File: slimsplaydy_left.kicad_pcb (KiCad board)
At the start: 2 copper layers, 122.6 x 97.5 mm, 37 parts

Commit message: some ideas and how-tos
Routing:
- net GND: track 50.8 -> 0.09 mm, vias 9 -> 16
- net finger_middle_bottom: track 122.0 -> 106.1 mm
- net finger_inner_home: track 71.0 -> 77.8 mm
- net BAT_P: track 68.7 -> 62.7 mm, vias 2 -> 4
- net thumb_tucky_fan: track 61.6 -> 64.2 mm
- net RAW: track 69.8 -> 71.8 mm, vias 2 -> 4
- net finger_inner_top: track 17.2 -> 15.4 mm
- net finger_index_bottom: track 78.6 -> 80.1 mm
- net thumb_reachy_fan: track 47.2 -> 48.4 mm
- net RST: track 64.1 -> 63.3 mm
- net finger_pinky_bottom: track 142.8 -> 143.3 mm
- added copper zone on F.Cu, net BAT_P
- added copper zone on B.Cu, net RAW
- added copper zone on F.Cu, net RAW
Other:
- outline, holes or cut-outs redrawn

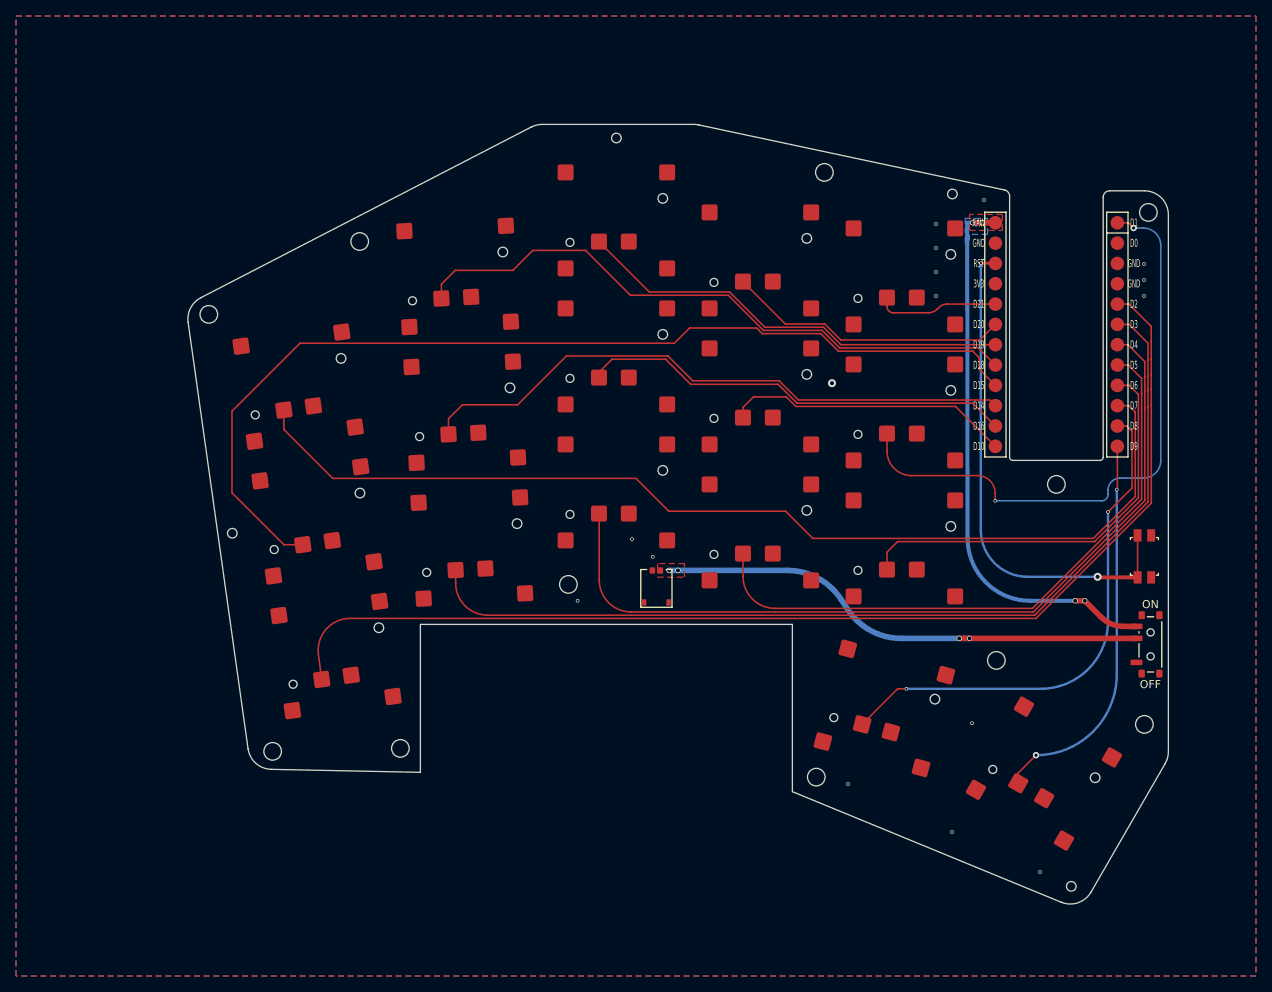
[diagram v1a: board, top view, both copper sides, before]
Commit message: fixed cutout
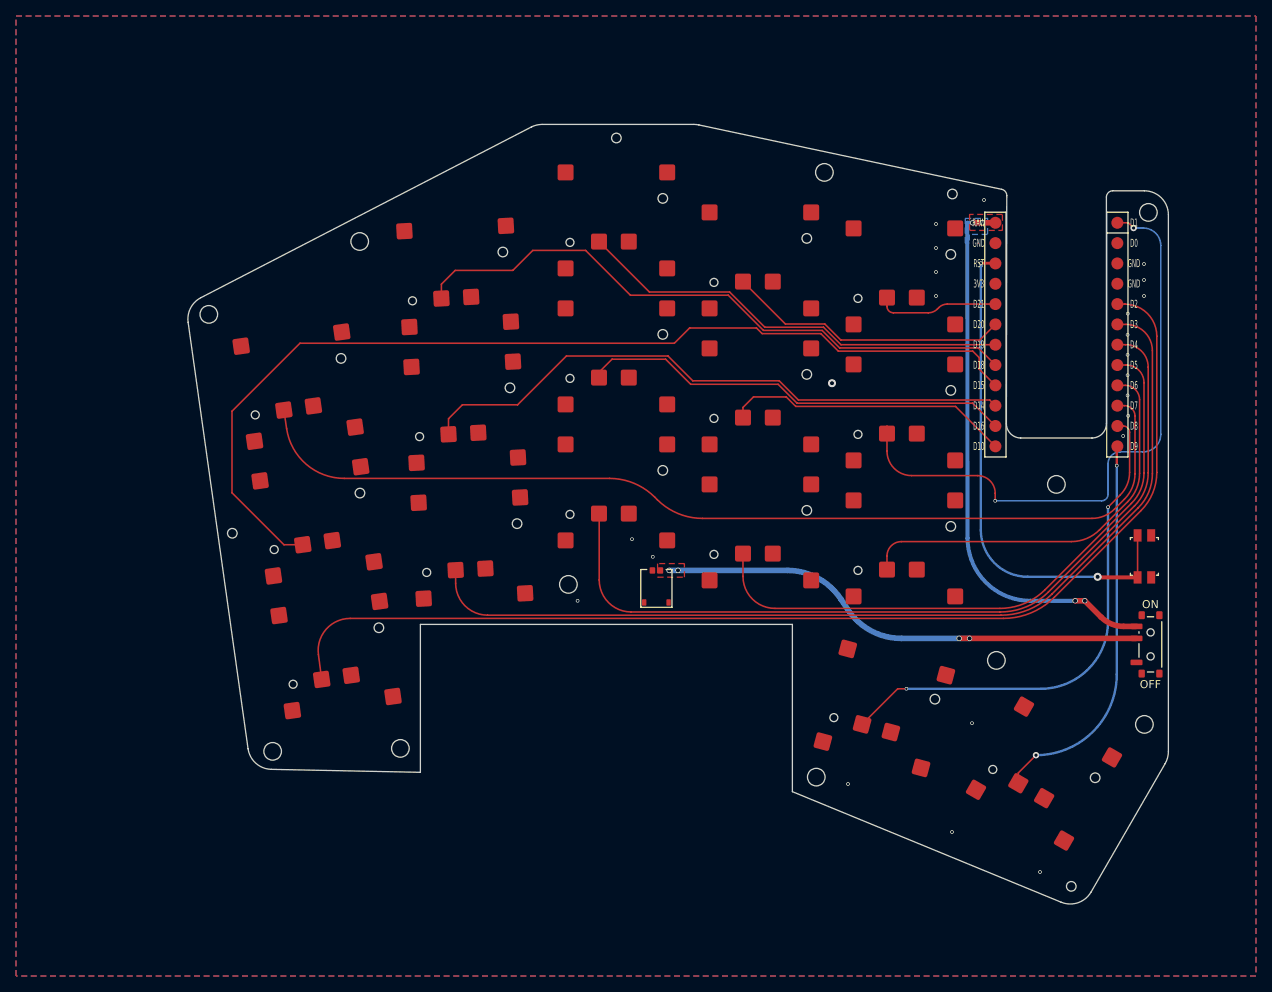
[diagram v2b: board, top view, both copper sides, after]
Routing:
- net finger_pinky_top: track 129.8 -> 125.7 mm
- net finger_inner_home: track 77.8 -> 81.1 mm
- net finger_inner_bottom: track 52.4 -> 51.4 mm
- net finger_index_bottom: track 80.1 -> 79.3 mm
- net thumb_tucky_fan: track 64.2 -> 63.6 mm
- net finger_middle_bottom: track 106.1 -> 105.6 mm
- net GND: vias 16 -> 23
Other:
- outline, holes or cut-outs redrawn

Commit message: rerouted tracks, stitched ground, fixed footprints, fixed mcu clearance
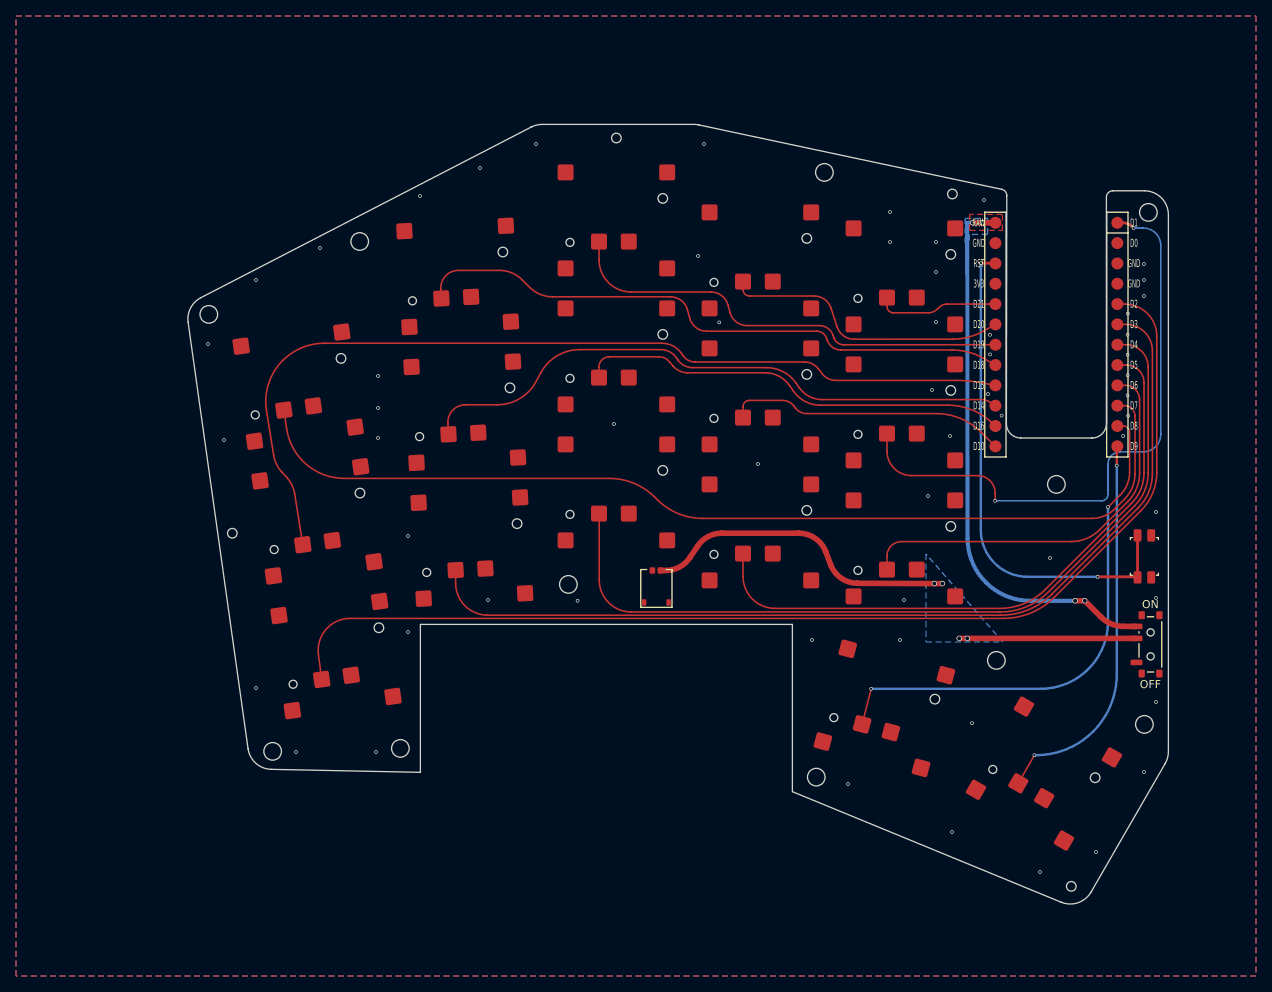
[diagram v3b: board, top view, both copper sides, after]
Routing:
- net finger_pinky_home: track 125.3 -> 115.7 mm
- net finger_ring_top: track 78.7 -> 76.4 mm
- net finger_middle_top: track 54.9 -> 57.2 mm
- net thumb_tucky_fan: track 63.6 -> 65.2 mm
- net finger_inner_home: track 81.1 -> 80.0 mm
- net finger_index_top: track 35.4 -> 36.3 mm
- net finger_index_home: track 35.9 -> 35.2 mm
- net BAT_P: track 62.7 -> 62.2 mm
- net GND: track 0.09 -> 0.00 mm, vias 23 -> 58
- added copper zone on B.Cu, net BAT_P
- removed copper zone on F.Cu, net BAT_P
